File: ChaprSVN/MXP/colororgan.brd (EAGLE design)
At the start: 76.2 x 50.8 mm, 42 parts, among them Q1 2N3904, Q2 2N3906, Q3 2N3906, Q4 2N3906, X1 057-034-1, X2 057-034-1

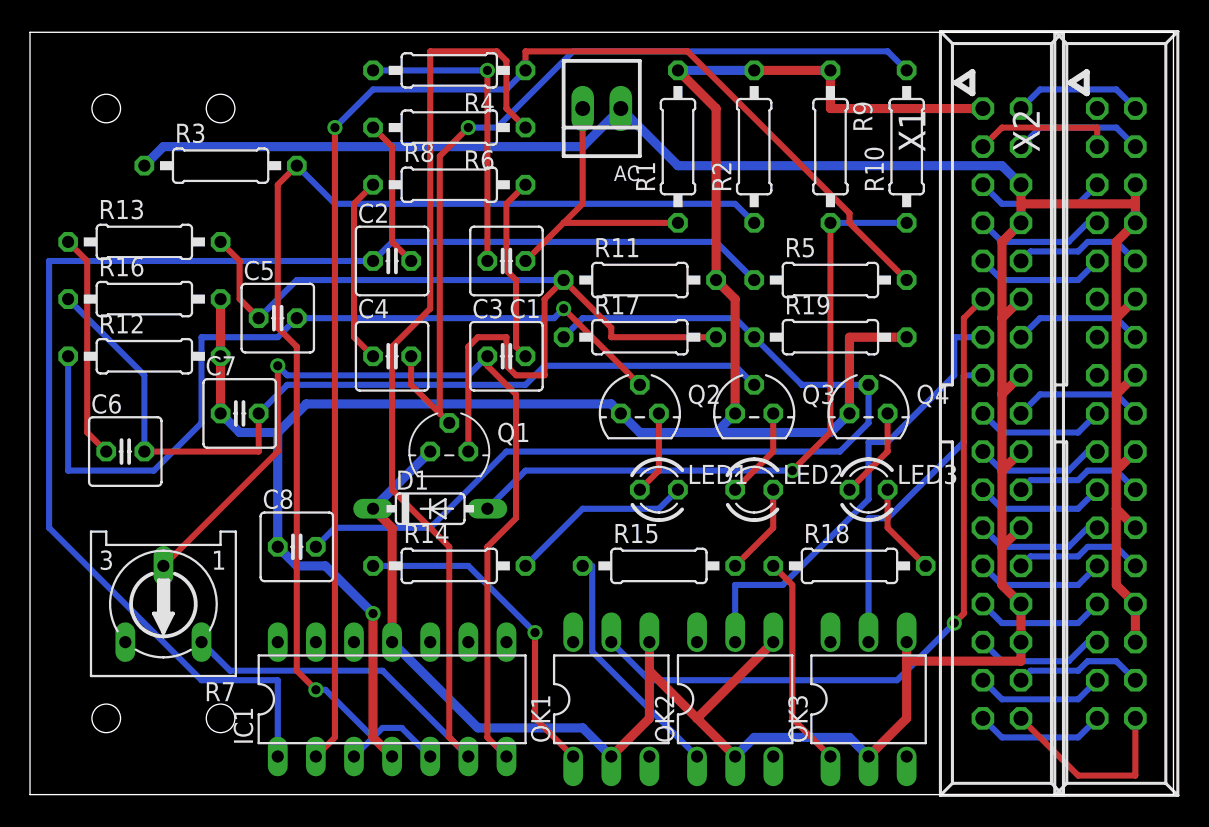
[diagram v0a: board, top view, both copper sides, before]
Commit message: A few changes for ease of reading. added 5v to the upward bound MXP connector.
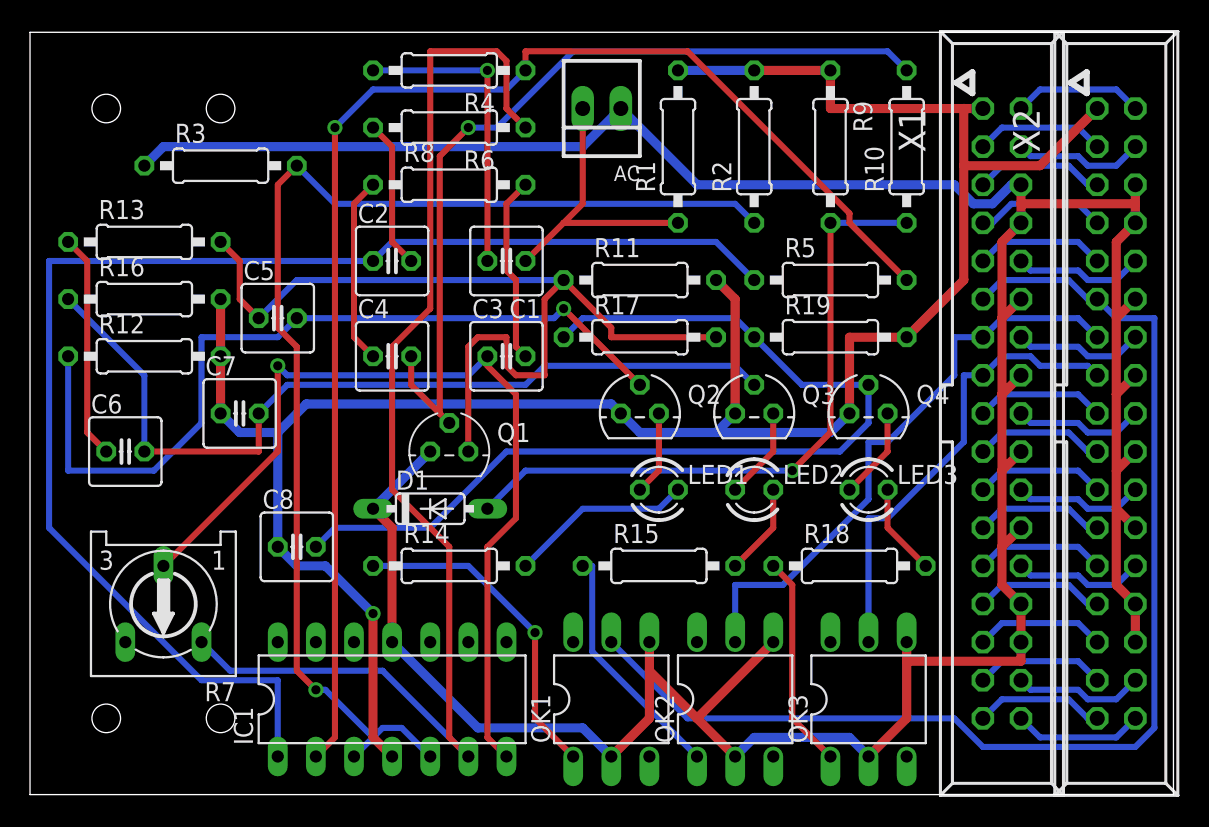
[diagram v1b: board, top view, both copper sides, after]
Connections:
- net +5V: now also X2.1
- net N$20: now also X2.11
- net N$24: now also X2.13
- net N$29: now also X2.15
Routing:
- net N$20: track 47.9 -> 79.9 mm, vias 1 -> 0
- net +5V: track 136.0 -> 148.3 mm
- net N$24: track 30.9 -> 39.6 mm
- net N$29: track 22.4 -> 31.1 mm
- net N$30: track 13.0 -> 8.67 mm
- net GND: track 231.2 -> 232.2 mm
- net N$39: track 9.42 -> 8.67 mm
